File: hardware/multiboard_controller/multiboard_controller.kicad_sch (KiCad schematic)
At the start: 0 parts

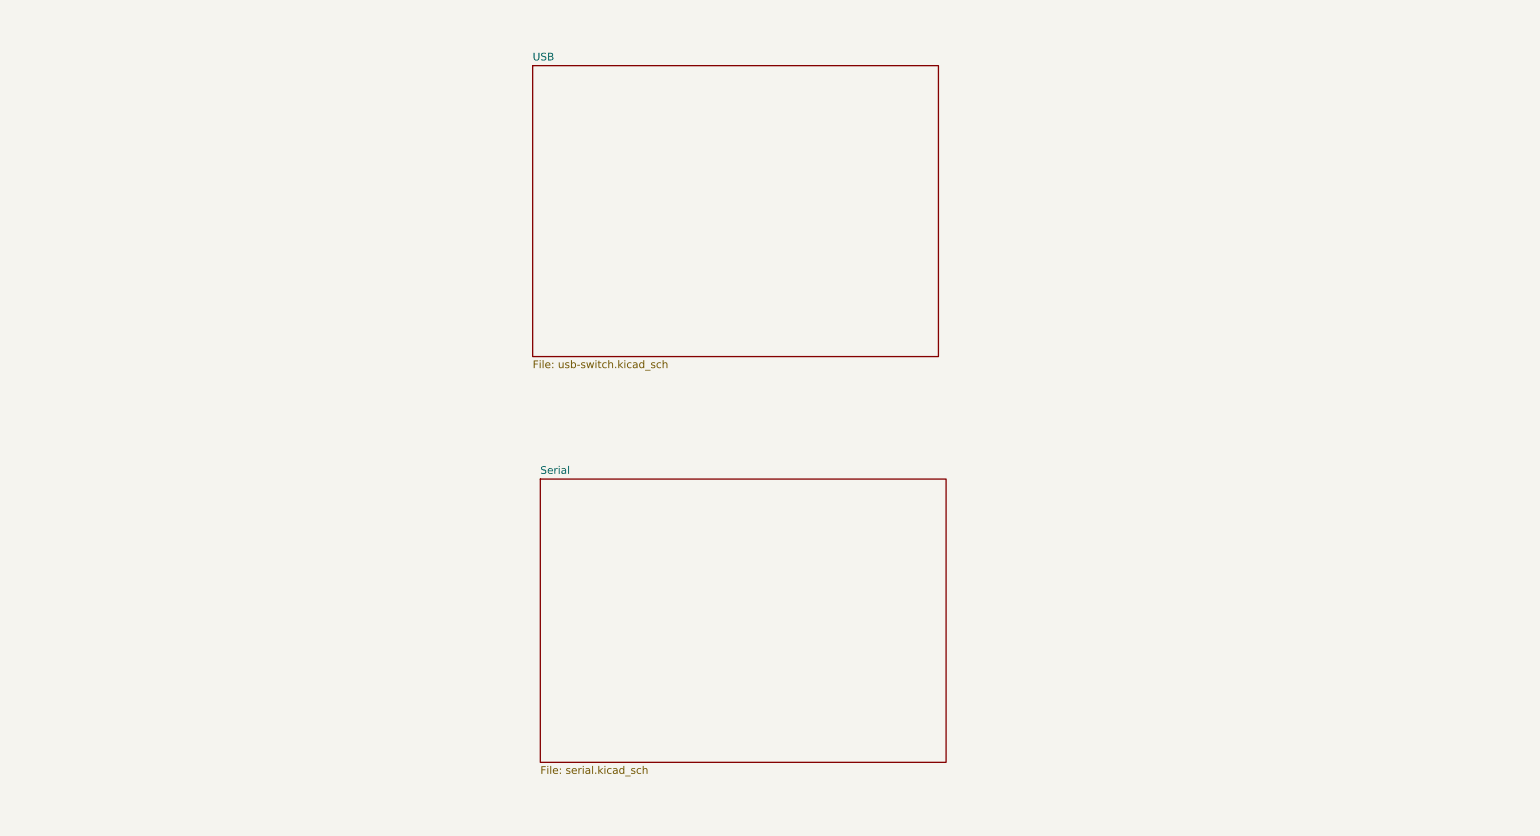
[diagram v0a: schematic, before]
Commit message: Adding USB Connector for Power and Data
First USB connector is for power and data input from the host. Power is taken from the V_BUS line and stepped to 3V3 to power other components using an LDO. Updated block diagram accordingly.
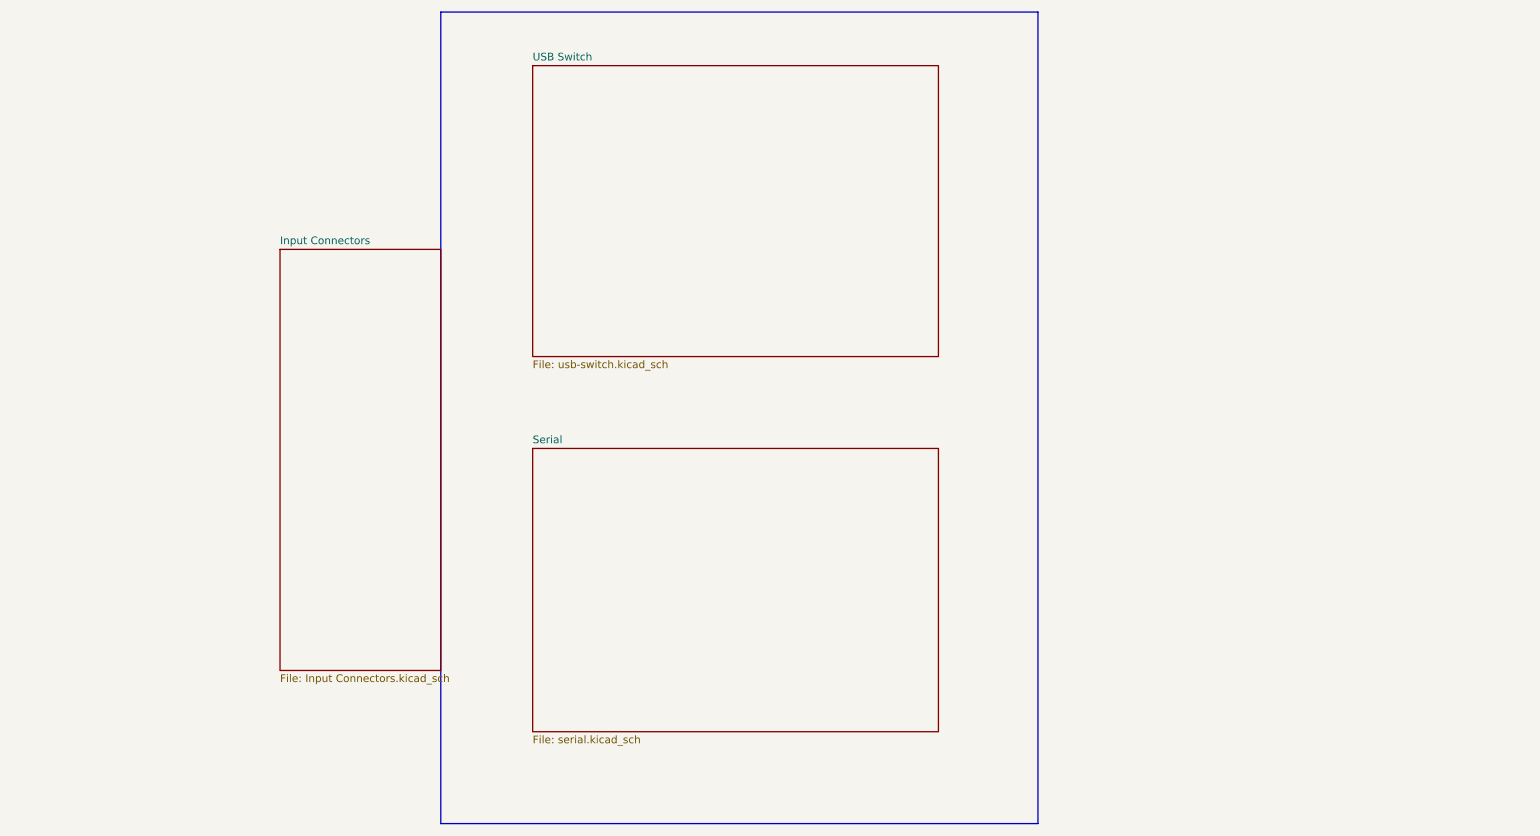
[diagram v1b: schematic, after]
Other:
- sheet USB renamed USB Switch
- added sheet Input Connectors (Input Connectors.kicad_sch)
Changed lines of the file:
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@@
 	(generator_version "8.0")
 	(paper "A4")
+	(rectangle
+		(start 90.17 17.78)
+		(end 189.23 152.4)
+		(stroke
+			(width 0)
+			(type default)
+		)
+		(fill
+			(type none)
+		)
+	)
+	(sheet
+		(at 63.5 57.15)
+		(size 26.67 69.85)
+		(fields_autoplaced yes)
+		(stroke
+			(width 0.1524)
+			(type solid)
+		)
+		(fill
+			(color 0 0 0 0.0000)
+		)
+		(property "Sheetname" "Input Connectors"
+			(at 63.5 56.4384 0)
+			(effects
+				(font
+					(size 1.27 1.27)
+				)
+				(justify left bottom)
+			)
+		)
+		(property "Sheetfile" "Input Connectors.kicad_sch"
+			(at 63.5 127.5846 0)
+			(effects
+				(font
+					(size 1.27 1.27)
+				)
+				(justify left top)
+			)
+		)
+		(instances
+			(project "multiboard_controller"
+				(path "/0fe19ce7-810a-40c6-903d-4212edc122f9"
+					(page "4")
+				)
+			)
+		)
+	)
 	(sheet
 		(at 105.41 26.67)
@@
 			(color 0 0 0 0.0000)
 		)
-		(property "Sheetname" "USB"
+		(property "Sheetname" "USB Switch"
 			(at 105.41 25.9584 0)
 			(effects
@@
 		)
 		(instances
-			(project "multiboard-controller"
+			(project "multiboard_controller"
 				(path "/0fe19ce7-810a-40c6-903d-4212edc122f9"
 					(page "2")
@@
 	)
 	(sheet
-		(at 106.68 95.25)
+		(at 105.41 90.17)
 		(size 67.31 46.99)
 		(fields_autoplaced yes)
@@
 		)
 		(property "Sheetname" "Serial"
-			(at 106.68 94.5384 0)
+			(at 105.41 89.4584 0)
 			(effects
 				(font
@@
 		)
 		(property "Sheetfile" "serial.kicad_sch"
-			(at 106.68 142.8246 0)
+			(at 105.41 137.7446 0)
 			(effects
 				(font
@@
 		)
 		(instances
-			(project "multiboard-controller"
+			(project "multiboard_controller"
 				(path "/0fe19ce7-810a-40c6-903d-4212edc122f9"
 					(page "3")

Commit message: Add Channel Select switches and USB output ports
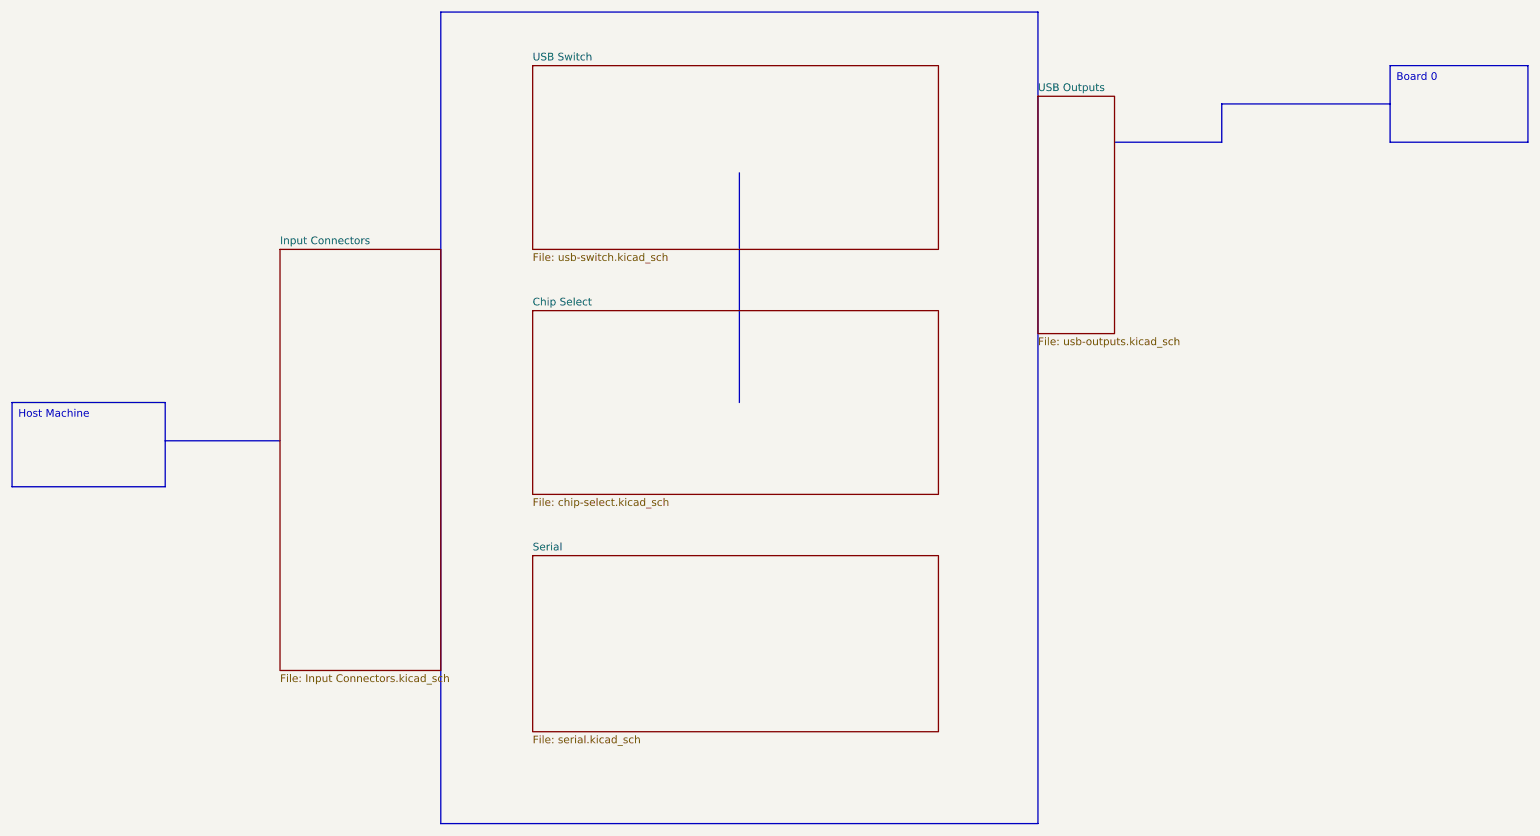
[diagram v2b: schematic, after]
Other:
- added sheet Chip Select (chip-select.kicad_sch)
- added sheet USB Outputs (usb-outputs.kicad_sch)
- title: (none) -> Multiboard Controller
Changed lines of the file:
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@@
 	(generator_version "8.0")
 	(paper "A4")
+	(title_block
+		(title "Multiboard Controller")
+		(date "2025-02-12")
+	)
+	(polyline
+		(pts
+			(xy 219.71 39.37) (xy 219.71 33.02)
+		)
+		(stroke
+			(width 0)
+			(type default)
+		)
+	)
+	(polyline
+		(pts
+			(xy 44.45 88.9) (xy 63.5 88.9)
+		)
+		(stroke
+			(width 0)
+			(type default)
+		)
+	)
+	(polyline
+		(pts
+			(xy 139.7 44.45) (xy 139.7 82.55)
+		)
+		(stroke
+			(width 0)
+			(type default)
+		)
+	)
+	(polyline
+		(pts
+			(xy 219.71 33.02) (xy 247.65 33.02)
+		)
+		(stroke
+			(width 0)
+			(type default)
+		)
+	)
+	(polyline
+		(pts
+			(xy 201.93 39.37) (xy 219.71 39.37)
+		)
+		(stroke
+			(width 0)
+			(type default)
+		)
+	)
 	(rectangle
 		(start 90.17 17.78)
@@
 		)
 	)
+	(text_box "Board 0"
+		(exclude_from_sim no)
+		(at 247.65 26.67 0)
+		(size 22.86 12.7)
+		(stroke
+			(width 0)
+			(type default)
+		)
+		(fill
+			(type none)
+		)
+		(effects
+			(font
+				(size 1.27 1.27)
+			)
+			(justify left top)
+		)
+	)
+	(text_box "Host Machine"
+		(exclude_from_sim no)
+		(at 19.05 82.55 0)
+		(size 25.4 13.97)
+		(stroke
+			(width 0)
+			(type default)
+		)
+		(fill
+			(type none)
+		)
+		(effects
+			(font
+				(size 1.27 1.27)
+			)
+			(justify left top)
+		)
+	)
 	(sheet
 		(at 63.5 57.15)
@@
 	)
 	(sheet
+		(at 189.23 31.75)
+		(size 12.7 39.37)
+		(fields_autoplaced yes)
+		(stroke
+			(width 0.1524)
+			(type solid)
+		)
+		(fill
+			(color 0 0 0 0.0000)
+		)
+		(property "Sheetname" "USB Outputs"
+			(at 189.23 31.0384 0)
+			(effects
+				(font
+					(size 1.27 1.27)
+				)
+				(justify left bottom)
+			)
+		)
+		(property "Sheetfile" "usb-outputs.kicad_sch"
+			(at 189.23 71.7046 0)
+			(effects
+				(font
+					(size 1.27 1.27)
+				)
+				(justify left top)
+			)
+		)
+		(instances
+			(project "multiboard_controller"
+				(path "/0fe19ce7-810a-40c6-903d-4212edc122f9"
+					(page "5")
+				)
+			)
+		)
+	)
+	(sheet
 		(at 105.41 26.67)
-		(size 67.31 48.26)
+		(size 67.31 30.48)
 		(fields_autoplaced yes)
 		(stroke
@@
 		)
 		(property "Sheetfile" "usb-switch.kicad_sch"
-			(at 105.41 75.5146 0)
+			(at 105.41 57.7346 0)
 			(effects
 				(font
@@
 	)
 	(sheet
-		(at 105.41 90.17)
-		(size 67.31 46.99)
+		(at 105.41 107.95)
+		(size 67.31 29.21)
 		(fields_autoplaced yes)
 		(stroke
@@
 		)
 		(property "Sheetname" "Serial"
-			(at 105.41 89.4584 0)
+			(at 105.41 107.2384 0)
 			(effects
 				(font
@@
 				)
 			)
+		)
+	)
+	(sheet
+		(at 105.41 67.31)
+		(size 67.31 30.48)
+		(fields_autoplaced yes)
+		(stroke
+			(width 0.1524)
+			(type solid)
+		)
+		(fill
+			(color 0 0 0 0.0000)
+		)
+		(property "Sheetname" "Chip Select"
+			(at 105.41 66.5984 0)
+			(effects
+				(font
+					(size 1.27 1.27)
+				)
+				(justify left bottom)
+			)
+		)
+		(property "Sheetfile" "chip-select.kicad_sch"
+			(at 105.41 98.3746 0)
+			(effects
+				(font
+					(size 1.27 1.27)
+				)
+				(justify left top)
+			)
+		)
+		(instances
+			(project "multiboard_controller"
+				(path "/0fe19ce7-810a-40c6-903d-4212edc122f9"
+					(page "6")
+				)
+			)

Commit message: Creating serial outputs.
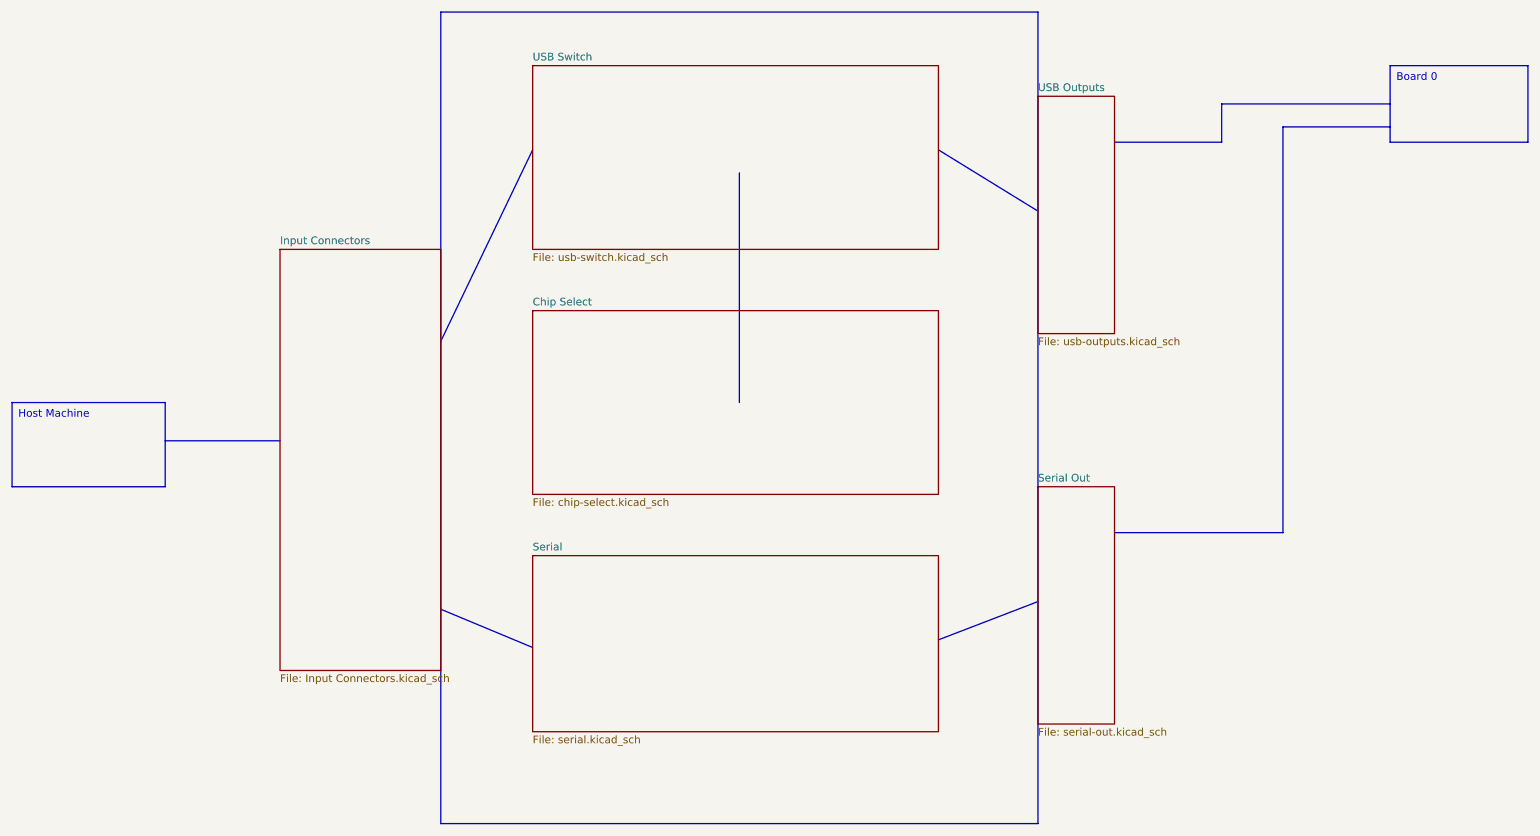
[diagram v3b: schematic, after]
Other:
- added sheet Serial Out (serial-out.kicad_sch)
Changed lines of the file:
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@@
+	(polyline
+		(pts
+			(xy 90.17 72.39) (xy 105.41 40.64)
+		)
+		(stroke
+			(width 0)
+			(type default)
+		)
+	)
+	(polyline
+		(pts
+			(xy 90.17 116.84) (xy 105.41 123.19)
+		)
+		(stroke
+			(width 0)
+			(type default)
+		)
+	)
 	(polyline
 		(pts
@@
 	(polyline
 		(pts
+			(xy 172.72 121.92) (xy 189.23 115.57)
+		)
+		(stroke
+			(width 0)
+			(type default)
+		)
+	)
+	(polyline
+		(pts
+			(xy 229.87 36.83) (xy 247.65 36.83)
+		)
+		(stroke
+			(width 0)
+			(type default)
+		)
+	)
+	(polyline
+		(pts
+			(xy 172.72 40.64) (xy 189.23 50.8)
+		)
+		(stroke
+			(width 0)
+			(type default)
+		)
+	)
+	(polyline
+		(pts
+			(xy 229.87 104.14) (xy 229.87 36.83)
+		)
+		(stroke
+			(width 0)
+			(type default)
+		)
+	)
+	(polyline
+		(pts
 			(xy 139.7 44.45) (xy 139.7 82.55)
+		)
+		(stroke
+			(width 0)
+			(type default)
+		)
+	)
+	(polyline
+		(pts
+			(xy 201.93 104.14) (xy 229.87 104.14)
 		)
 		(stroke
@@
 			(project "multiboard_controller"
 				(path "/0fe19ce7-810a-40c6-903d-4212edc122f9"
-					(page "4")
+					(page "2")
 				)
 			)
@@
 			(project "multiboard_controller"
 				(path "/0fe19ce7-810a-40c6-903d-4212edc122f9"
-					(page "2")
+					(page "4")
 				)
 			)
@@
 				)
 			)
+		)
+	)
+	(sheet
+		(at 189.23 96.52)
+		(size 12.7 39.37)
+		(fields_autoplaced yes)
+		(stroke
+			(width 0.1524)
+			(type solid)
+		)
+		(fill
+			(color 0 0 0 0.0000)
+		)
+		(property "Sheetname" "Serial Out"
+			(at 189.23 95.8084 0)
+			(effects
+				(font
+					(size 1.27 1.27)
+				)
+				(justify left bottom)
+			)
+		)
+		(property "Sheetfile" "serial-out.kicad_sch"
+			(at 189.23 136.4746 0)
+			(effects
+				(font
+					(size 1.27 1.27)
+				)
+				(justify left top)
+			)
+		)
+		(instances
+			(project "multiboard_controller"
+				(path "/0fe19ce7-810a-40c6-903d-4212edc122f9"
+					(page "7")
+				)
+			)

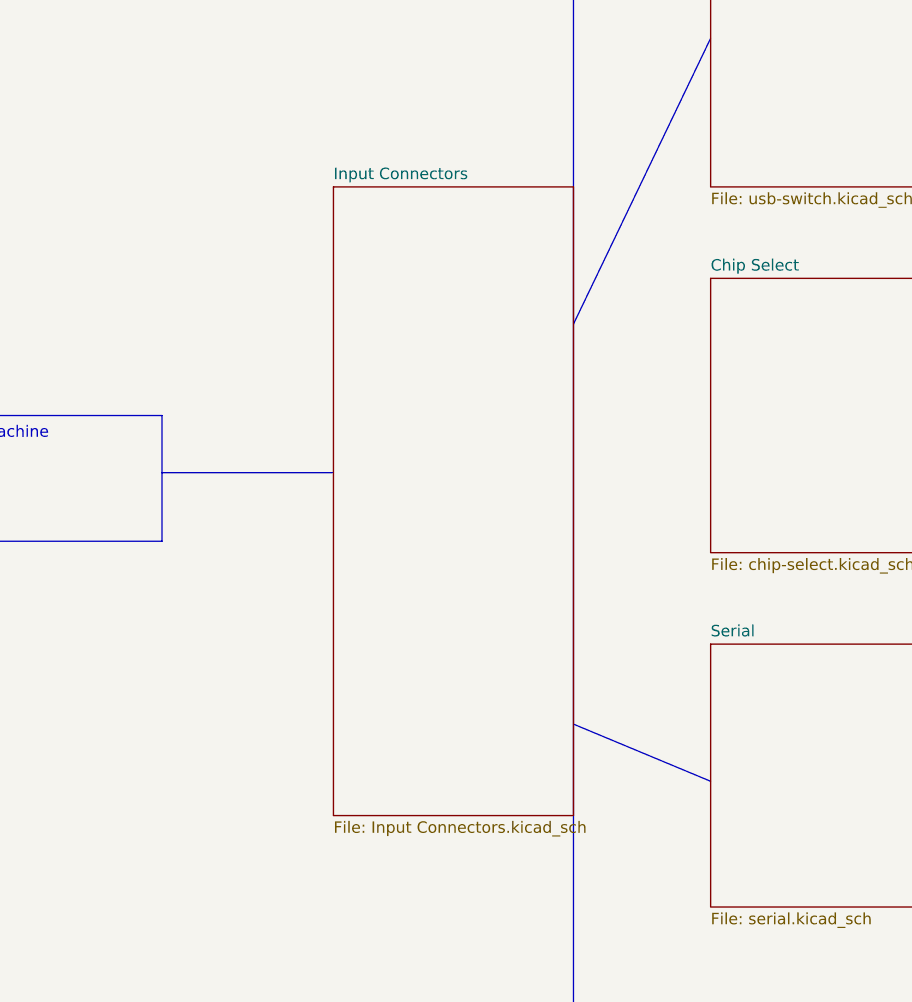
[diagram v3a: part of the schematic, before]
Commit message: Choose switches for UART muxing. USB-to-UART schematic WIP.
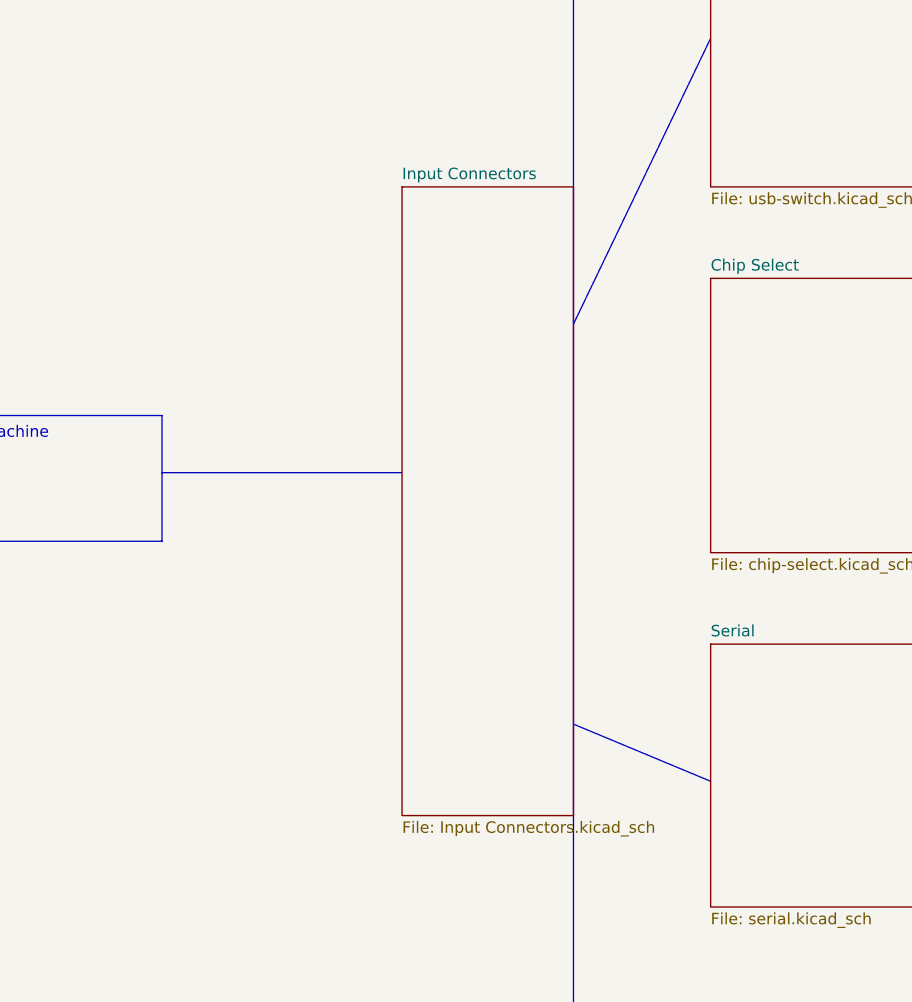
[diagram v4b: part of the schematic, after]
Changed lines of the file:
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@@
 	(polyline
 		(pts
-			(xy 44.45 88.9) (xy 63.5 88.9)
+			(xy 44.45 88.9) (xy 71.12 88.9)
 		)
 		(stroke
@@
 	)
 	(sheet
-		(at 63.5 57.15)
-		(size 26.67 69.85)
+		(at 71.12 57.15)
+		(size 19.05 69.85)
 		(fields_autoplaced yes)
 		(stroke
@@
 		)
 		(property "Sheetname" "Input Connectors"
-			(at 63.5 56.4384 0)
+			(at 71.12 56.4384 0)
 			(effects
 				(font
@@
 		)
 		(property "Sheetfile" "Input Connectors.kicad_sch"
-			(at 63.5 127.5846 0)
+			(at 71.12 127.5846 0)
 			(effects
 				(font
